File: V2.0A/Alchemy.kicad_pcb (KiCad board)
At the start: 4 copper layers, 55 x 85 mm, 65 parts, among them J1 Conn_02x20_Odd_Even, J2 USB_C_Receptacle_USB2.0, J3 USB_C_Receptacle_USB2.0, J4 Conn_01x03, J5 Conn_01x03, J6 Conn_01x02, J7 Conn_01x02, J8 Conn_01x02, J9 Conn_01x03, U1 CH32V203C8T6, U2 LM5164DDA, U3 CH213K, U4 AMS1117-3.3, U5 CH213K, U6 MT9700, Y2 8MHz

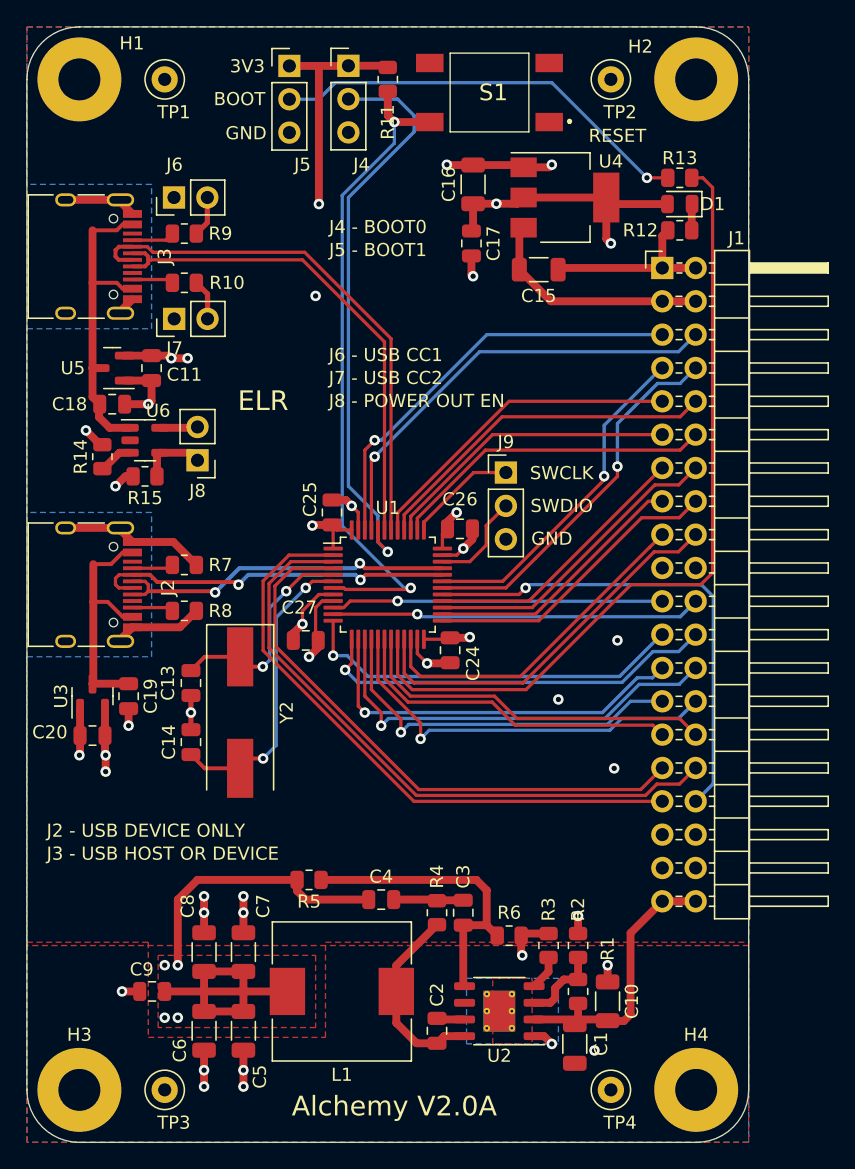
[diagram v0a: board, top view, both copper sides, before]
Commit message: Minor layout fixes
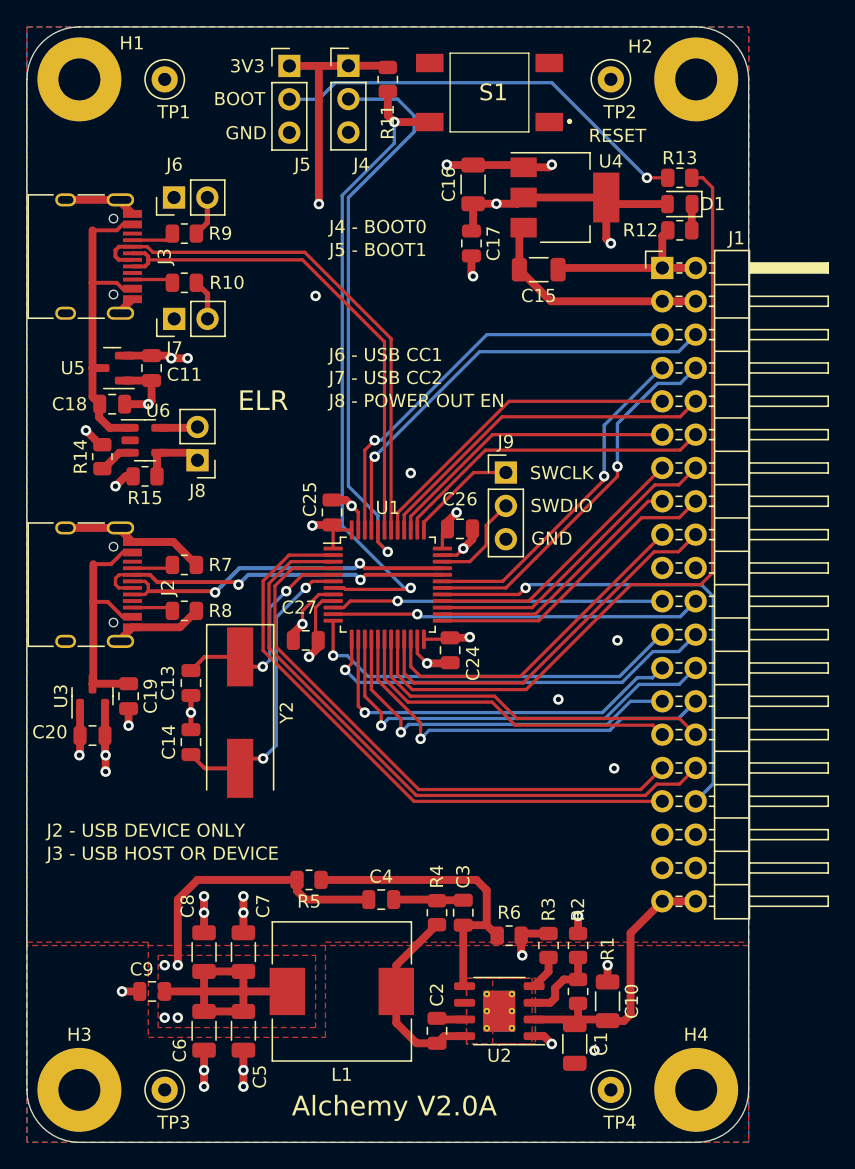
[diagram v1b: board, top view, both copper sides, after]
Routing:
- net GND: vias 31 -> 32
- added copper zone on In2.Cu, net GND
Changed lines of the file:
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@@
       (drillshape 0)
       (scaleselection 1)
-      (outputdirectory "gerber/")
+      (outputdirectory "Gerber/")
     )
   )
@@
     (fp_line (start 1 0.625) (end -1 0.625) (layer "F.Fab") (width 0.1))
     (fp_line (start -1 0.625) (end -1 -0.625) (layer "F.Fab") (width 0.1))
-    (pad "1" smd roundrect (at -0.9125 0 90) (size 1.025 1.4) (layers "F.Cu" "F.Paste" "F.Mask") (roundrect_rratio 0.243902)
+    (pad "1" smd roundrect (at -0.9125 0 90) (size 1.025 1.4) (layers "F.Cu" "F.Paste" "F.Mask") (roundrect_rratio 0.243902439)
       (net 51 "Net-(R14-Pad1)") (pintype "passive"))
-    (pad "2" smd roundrect (at 0.9125 0 90) (size 1.025 1.4) (layers "F.Cu" "F.Paste" "F.Mask") (roundrect_rratio 0.243902)
+    (pad "2" smd roundrect (at 0.9125 0 90) (size 1.025 1.4) (layers "F.Cu" "F.Paste" "F.Mask") (roundrect_rratio 0.243902439)
       (net 60 "GND") (pintype "passive"))
     (model "${KICAD6_3DMODEL_DIR}/Resistor_SMD.3dshapes/R_0805_2012Metric.wrl"
@@
     (fp_line (start 1 0.625) (end -1 0.625) (layer "F.Fab") (width 0.1))
     (fp_line (start 1 -0.625) (end 1 0.625) (layer "F.Fab") (width 0.1))
-    (pad "1" smd roundrect (at -0.9125 0 180) (size 1.025 1.4) (layers "F.Cu" "F.Paste" "F.Mask") (roundrect_rratio 0.243902)
+    (pad "1" smd roundrect (at -0.9125 0 180) (size 1.025 1.4) (layers "F.Cu" "F.Paste" "F.Mask") (roundrect_rratio 0.243902439)
       (net 68 "Net-(J8-Pad1)") (pintype "passive"))
-    (pad "2" smd roundrect (at 0.9125 0 180) (size 1.025 1.4) (layers "F.Cu" "F.Paste" "F.Mask") (roundrect_rratio 0.243902)
+    (pad "2" smd roundrect (at 0.9125 0 180) (size 1.025 1.4) (layers "F.Cu" "F.Paste" "F.Mask") (roundrect_rratio 0.243902439)
       (net 60 "GND") (pintype "passive"))
     (model "${KICAD6_3DMODEL_DIR}/Resistor_SMD.3dshapes/R_0805_2012Metric.wrl"
@@
     (fp_line (start -1.6 -0.8) (end 1.6 -0.8) (layer "F.Fab") (width 0.1))
     (fp_line (start -1.6 0.8) (end -1.6 -0.8) (layer "F.Fab") (width 0.1))
-    (pad "1" smd roundrect (at -1.475 0 270) (size 1.15 1.8) (layers "F.Cu" "F.Paste" "F.Mask") (roundrect_rratio 0.217391)
+    (pad "1" smd roundrect (at -1.475 0 270) (size 1.15 1.8) (layers "F.Cu" "F.Paste" "F.Mask") (roundrect_rratio 0.2173913043)
       (net 60 "GND") (pintype "passive"))
-    (pad "2" smd roundrect (at 1.475 0 270) (size 1.15 1.8) (layers "F.Cu" "F.Paste" "F.Mask") (roundrect_rratio 0.217391)
+    (pad "2" smd roundrect (at 1.475 0 270) (size 1.15 1.8) (layers "F.Cu" "F.Paste" "F.Mask") (roundrect_rratio 0.2173913043)
       (net 61 "/VM") (pintype "passive"))
     (model "${KICAD6_3DMODEL_DIR}/Capacitor_SMD.3dshapes/C_1206_3216Metric.wrl"
@@
   (via (at 164 122.75) (size 0.8) (drill 0.4) (layers "F.Cu" "B.Cu") (free) (net 60))
   (via (at 155.25 94.75) (size 0.8) (drill 0.4) (layers "F.Cu" "B.Cu") (free) (net 60))
+  (via (at 151.25 89) (size 0.8) (drill 0.4) (layers "F.Cu" "B.Cu") (free) (net 60))
   (via (at 166.75 111.5) (size 0.8) (drill 0.4) (layers "F.Cu" "B.Cu") (free) (net 60))
   (via (at 154 65.5) (size 0.8) (drill 0.4) (layers "F.Cu" "B.Cu") (free) (net 60))
@@
   (segment (start 153.6625 95.75) (end 155.75 95.75) (width 0.25) (layer "F.Cu") (net 70))
   (segment (start 157 94.5) (end 157 93) (width 0.25) (layer "F.Cu") (net 70))
+  (zone (net 60) (net_name "GND") (layers "F.Cu" "In1.Cu" "In2.Cu" "B.Cu") (hatch edge 0.508)
+    (priority 1)
+    (connect_pads yes (clearance 0.4))
+    (min_thickness 0.254) (filled_areas_thickness no)
+    (fill yes (thermal_gap 0.508) (thermal_bridge_width 0.508))
+    (polygon
+      (pts
+        (xy 160.75 132.5)
+        (xy 155.5 132.5)
+        (xy 155.5 127.5)
+        (xy 160.75 127.5)
+      )
+    )
+  )
   (zone (net 60) (net_name "GND") (layer "F.Cu") (hatch edge 0.508)
     (connect_pads thru_hole_only (clearance 0.508))
@@
   )
   (zone (net 60) (net_name "GND") (layer "B.Cu") (hatch edge 0.508)
-    (connect_pads yes (clearance 0.508))
-    (min_thickness 0.254) (filled_areas_thickness no)
-    (fill yes (thermal_gap 0.508) (thermal_bridge_width 0.508))
-    (polygon
-      (pts
-        (xy 162.5 132.5)
-        (xy 155.5 132.5)
-        (xy 155.5 127.5)
-        (xy 162.5 127.5)
-      )
-    )
-  )
-  (zone (net 60) (net_name "GND") (layer "B.Cu") (hatch edge 0.508)
     (connect_pads thru_hole_only (clearance 0.508))
     (min_thickness 0.254) (filled_areas_thickness no)
@@
         (xy 177 140)
         (xy 122 140)
-        (xy 122 103)
-        (xy 131.5 103)
-        (xy 131.5 92)
-        (xy 122 92)
-        (xy 122 78)
-        (xy 131.5 78)
-        (xy 131.5 67)
-        (xy 122 67)
         (xy 122 55)
         (xy 177 55)
